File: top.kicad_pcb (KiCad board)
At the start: 2 copper layers, 98 x 50 mm, 4 parts, among them J2 Conn_01x01_Male, J5 Conn_01x01_Male, J7 Conn_01x01_Male, J9 Conn_01x01_Male

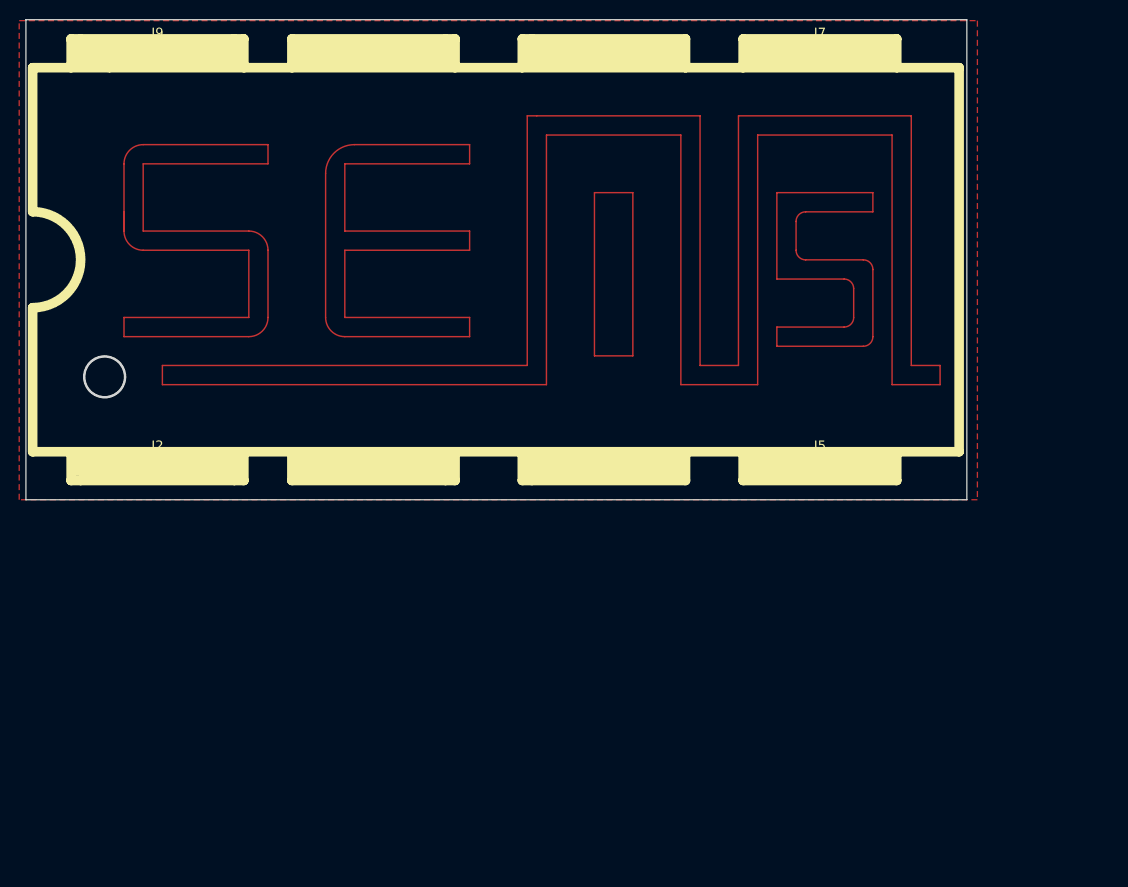
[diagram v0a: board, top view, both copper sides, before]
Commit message: top add silkscreen and fill other side
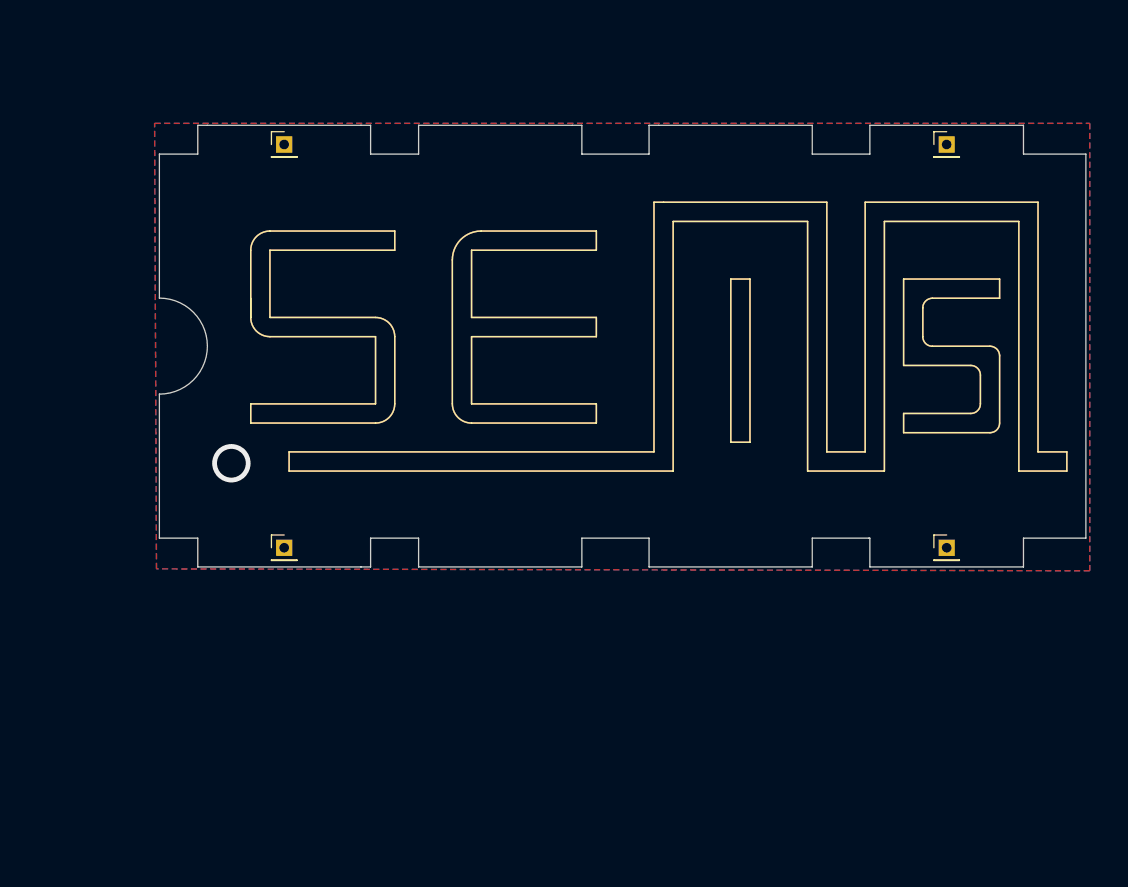
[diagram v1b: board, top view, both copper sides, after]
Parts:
- moved J9 16.1 mm to (95.7, 60.0)
- moved J7 16.1 mm to (164.7, 60.0)
- moved J2 15.6 mm to (95.7, 102.0)
- moved J5 15.6 mm to (164.7, 102.0)
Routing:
- added copper zone on B.Cu, net (none)
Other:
- board size 98 x 50 mm -> 96.5 x 46 mm

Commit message: gerberek, bom
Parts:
- added T1: Tab, kikit:Tab, F.Cu at (82.2, 68.0)
- added T1: Tab, kikit:Tab, F.Cu at (164.8, 57.6)
- added T1: Tab, kikit:Tab, F.Cu at (82.2, 94.0)
- added T1: Tab, kikit:Tab, F.Cu at (179.8, 94.0)
- added T1: Tab, kikit:Tab, F.Cu at (95.8, 57.6)
- added T1: Tab, kikit:Tab, F.Cu at (95.8, 104.3)
- added T1: Tab, kikit:Tab, F.Cu at (164.8, 104.3)
- added T1: Tab, kikit:Tab, F.Cu at (179.6, 68.4)
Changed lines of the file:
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@@
     )
+  )
+  (footprint "kikit:Tab" (layer "F.Cu")
+    (at 82.25 68)
+    (descr "A symbol representing annotation for tab placement")
+    (property "Sheetfile" "SEM15.kicad_sch")
+    (property "Sheetname" "")
+    (property "exclude_from_bom" "")
+    (property "ki_description" "KiKit tab annotations")
+    (property "ki_keywords" "KiKit")
+    (attr exclude_from_pos_files exclude_from_bom)
+    (fp_text reference "T1" (at 0 -2) (layer "F.SilkS") hide
+        (effects (font (size 1 1) (thickness 0.15)))
+    )
+    (fp_text value "Tab" (at -2.75 -1) (layer "Dwgs.User")
+        (effects (font (size 1.2 1.2) (thickness 0.2)))
+    )
+    (fp_text user "KIKIT: width: 3mm" (at -5.5 0 90) (layer "Dwgs.User")
+        (effects (font (size 1 1) (thickness 0.15)))
+    )
+    (fp_line (start 0.25 0) (end -2.75 0)
+      (stroke (width 0.3) (type solid)) (layer "Dwgs.User"))
+    (fp_line (start 0.25 0) (end -0.75 -1)
+      (stroke (width 0.3) (type solid)) (layer "Dwgs.User"))
+    (fp_line (start 0.25 0) (end -0.75 1)
+      (stroke (width 0.3) (type solid)) (layer "Dwgs.User"))
+    (fp_line (start 0.25 1) (end 0.25 -1)
+      (stroke (width 0.3) (type solid)) (layer "Dwgs.User"))
+  )
+  (footprint "kikit:Tab" (layer "F.Cu")
+    (at 164.8 57.65 -90)
+    (descr "A symbol representing annotation for tab placement")
+    (property "Sheetfile" "SEM15.kicad_sch")
+    (property "Sheetname" "")
+    (property "exclude_from_bom" "")
+    (property "ki_description" "KiKit tab annotations")
+    (property "ki_keywords" "KiKit")
+    (attr exclude_from_pos_files exclude_from_bom)
+    (fp_text reference "T1" (at 0 -2 90) (layer "F.SilkS") hide
+        (effects (font (size 1 1) (thickness 0.15)))
+    )
+    (fp_text value "Tab" (at -2.75 -1 90) (layer "Dwgs.User")
+        (effects (font (size 1.2 1.2) (thickness 0.2)))
+    )
+    (fp_text user "KIKIT: width: 3mm" (at -5.5 0) (layer "Dwgs.User")
+        (effects (font (size 1 1) (thickness 0.15)))
+    )
+    (fp_line (start 0.25 0) (end -2.75 0)
+      (stroke (width 0.3) (type solid)) (layer "Dwgs.User"))
+    (fp_line (start 0.25 0) (end -0.75 -1)
+      (stroke (width 0.3) (type solid)) (layer "Dwgs.User"))
+    (fp_line (start 0.25 0) (end -0.75 1)
+      (stroke (width 0.3) (type solid)) (layer "Dwgs.User"))
+    (fp_line (start 0.25 1) (end 0.25 -1)
+      (stroke (width 0.3) (type solid)) (layer "Dwgs.User"))
+  )
+  (footprint "kikit:Tab" (layer "F.Cu")
+    (at 82.25 94)
+    (descr "A symbol representing annotation for tab placement")
+    (property "Sheetfile" "SEM15.kicad_sch")
+    (property "Sheetname" "")
+    (property "exclude_from_bom" "")
+    (property "ki_description" "KiKit tab annotations")
+    (property "ki_keywords" "KiKit")
+    (attr exclude_from_pos_files exclude_from_bom)
+    (fp_text reference "T1" (at 0 -2) (layer "F.SilkS") hide
+        (effects (font (size 1 1) (thickness 0.15)))
+    )
+    (fp_text value "Tab" (at -2.75 -1) (layer "Dwgs.User")
+        (effects (font (size 1.2 1.2) (thickness 0.2)))
+    )
+    (fp_text user "KIKIT: width: 3mm" (at -5.5 0 90) (layer "Dwgs.User")
+        (effects (font (size 1 1) (thickness 0.15)))
+    )
+    (fp_line (start 0.25 0) (end -2.75 0)
+      (stroke (width 0.3) (type solid)) (layer "Dwgs.User"))
+    (fp_line (start 0.25 0) (end -0.75 -1)
+      (stroke (width 0.3) (type solid)) (layer "Dwgs.User"))
+    (fp_line (start 0.25 0) (end -0.75 1)
+      (stroke (width 0.3) (type solid)) (layer "Dwgs.User"))
+    (fp_line (start 0.25 1) (end 0.25 -1)
+      (stroke (width 0.3) (type solid)) (layer "Dwgs.User"))
+  )
+  (footprint "kikit:Tab" (layer "F.Cu")
+    (at 179.75 94 180)
+    (descr "A symbol representing annotation for tab placement")
+    (property "Sheetfile" "SEM15.kicad_sch")
+    (property "Sheetname" "")
+    (property "exclude_from_bom" "")
+    (property "ki_description" "KiKit tab annotations")
+    (property "ki_keywords" "KiKit")
+    (attr exclude_from_pos_files exclude_from_bom)
+    (fp_text reference "T1" (at 0 -2) (layer "F.SilkS") hide
+        (effects (font (size 1 1) (thickness 0.15)))
+    )
+    (fp_text value "Tab" (at -2.75 -1) (layer "Dwgs.User")
+        (effects (font (size 1.2 1.2) (thickness 0.2)))
+    )
+    (fp_text user "KIKIT: width: 3mm" (at -5.5 0 90) (layer "Dwgs.User")
+        (effects (font (size 1 1) (thickness 0.15)))
+    )
+    (fp_line (start 0.25 0) (end -2.75 0)
+      (stroke (width 0.3) (type solid)) (layer "Dwgs.User"))
+    (fp_line (start 0.25 0) (end -0.75 -1)
+      (stroke (width 0.3) (type solid)) (layer "Dwgs.User"))
+    (fp_line (start 0.25 0) (end -0.75 1)
+      (stroke (width 0.3) (type solid)) (layer "Dwgs.User"))
+    (fp_line (start 0.25 1) (end 0.25 -1)
+      (stroke (width 0.3) (type solid)) (layer "Dwgs.User"))
   )
   (footprint "Connector_PinHeader_2.54mm:PinHeader_1x01_P2.54mm_Vertical" (layer "F.Cu")
@@
     )
   )
+  (footprint "kikit:Tab" (layer "F.Cu")
+    (at 95.8 57.65 -90)
+    (descr "A symbol representing annotation for tab placement")
+    (property "Sheetfile" "SEM15.kicad_sch")
+    (property "Sheetname" "")
+    (property "exclude_from_bom" "")
+    (property "ki_description" "KiKit tab annotations")
+    (property "ki_keywords" "KiKit")
+    (attr exclude_from_pos_files exclude_from_bom)
+    (fp_text reference "T1" (at 0 -2 90) (layer "F.SilkS") hide
+        (effects (font (size 1 1) (thickness 0.15)))
+    )
+    (fp_text value "Tab" (at -2.75 -1 90) (layer "Dwgs.User")
+        (effects (font (size 1.2 1.2) (thickness 0.2)))
+    )
+    (fp_text user "KIKIT: width: 3mm" (at -5.5 0) (layer "Dwgs.User")
+        (effects (font (size 1 1) (thickness 0.15)))
+    )
+    (fp_line (start 0.25 0) (end -2.75 0)
+      (stroke (width 0.3) (type solid)) (layer "Dwgs.User"))
+    (fp_line (start 0.25 0) (end -0.75 -1)
+      (stroke (width 0.3) (type solid)) (layer "Dwgs.User"))
+    (fp_line (start 0.25 0) (end -0.75 1)
+      (stroke (width 0.3) (type solid)) (layer "Dwgs.User"))
+    (fp_line (start 0.25 1) (end 0.25 -1)
+      (stroke (width 0.3) (type solid)) (layer "Dwgs.User"))
+  )
   (footprint "Connector_PinHeader_2.54mm:PinHeader_1x01_P2.54mm_Vertical" (layer "F.Cu")
     (at 95.7 102)
@@
     )
   )
+  (footprint "kikit:Tab" (layer "F.Cu")
+    (at 95.8 104.35 90)
+    (descr "A symbol representing annotation for tab placement")
+    (property "Sheetfile" "SEM15.kicad_sch")
+    (property "Sheetname" "")
+    (property "exclude_from_bom" "")
+    (property "ki_description" "KiKit tab annotations")
+    (property "ki_keywords" "KiKit")
+    (attr exclude_from_pos_files exclude_from_bom)
+    (fp_text reference "T1" (at 0 -2 90) (layer "F.SilkS") hide
+        (effects (font (size 1 1) (thickness 0.15)))
+    )
+    (fp_text value "Tab" (at -2.75 -1 90) (layer "Dwgs.User")
+        (effects (font (size 1.2 1.2) (thickness 0.2)))
+    )
+    (fp_text user "KIKIT: width: 3mm" (at -5.5 0) (layer "Dwgs.User")
+        (effects (font (size 1 1) (thickness 0.15)))
+    )
+    (fp_line (start 0.25 0) (end -2.75 0)
+      (stroke (width 0.3) (type solid)) (layer "Dwgs.User"))
+    (fp_line (start 0.25 0) (end -0.75 -1)
+      (stroke (width 0.3) (type solid)) (layer "Dwgs.User"))
+    (fp_line (start 0.25 0) (end -0.75 1)
+      (stroke (width 0.3) (type solid)) (layer "Dwgs.User"))
+    (fp_line (start 0.25 1) (end 0.25 -1)
+      (stroke (width 0.3) (type solid)) (layer "Dwgs.User"))
+  )
+  (footprint "kikit:Tab" (layer "F.Cu")
+    (at 164.8 104.35 90)
+    (descr "A symbol representing annotation for tab placement")
+    (property "Sheetfile" "SEM15.kicad_sch")
+    (property "Sheetname" "")
+    (property "exclude_from_bom" "")
+    (property "ki_description" "KiKit tab annotations")
+    (property "ki_keywords" "KiKit")
+    (attr exclude_from_pos_files exclude_from_bom)
+    (fp_text reference "T1" (at 0 -2 90) (layer "F.SilkS") hide
+        (effects (font (size 1 1) (thickness 0.15)))
+    )
+    (fp_text value "Tab" (at -2.75 -1 90) (layer "Dwgs.User")
+        (effects (font (size 1.2 1.2) (thickness 0.2)))
+    )
+    (fp_text user "KIKIT: width: 3mm" (at -5.5 0) (layer "Dwgs.User")
+        (effects (font (size 1 1) (thickness 0.15)))
+    )
+    (fp_line (start 0.25 0) (end -2.75 0)
+      (stroke (width 0.3) (type solid)) (layer "Dwgs.User"))
+    (fp_line (start 0.25 0) (end -0.75 -1)
+      (stroke (width 0.3) (type solid)) (layer "Dwgs.User"))
+    (fp_line (start 0.25 0) (end -0.75 1)
+      (stroke (width 0.3) (type solid)) (layer "Dwgs.User"))
+    (fp_line (start 0.25 1) (end 0.25 -1)
+      (stroke (width 0.3) (type solid)) (layer "Dwgs.User"))
+  )
+  (footprint "kikit:Tab" (layer "F.Cu")
+    (at 179.55 68.4 180)
+    (descr "A symbol representing annotation for tab placement")
+    (property "Sheetfile" "SEM15.kicad_sch")
+    (property "Sheetname" "")
+    (property "exclude_from_bom" "")
+    (property "ki_description" "KiKit tab annotations")
+    (property "ki_keywords" "KiKit")
+    (attr exclude_from_pos_files exclude_from_bom)
+    (fp_text reference "T1" (at 0 -2) (layer "F.SilkS") hide
+        (effects (font (size 1 1) (thickness 0.15)))
+    )
+    (fp_text value "Tab" (at -2.75 -1) (layer "Dwgs.User")
+        (effects (font (size 1.2 1.2) (thickness 0.2)))
+    )
+    (fp_text user "KIKIT: width: 3mm" (at -5.5 0 90) (layer "Dwgs.User")
+        (effects (font (size 1 1) (thickness 0.15)))
+    )
+    (fp_line (start 0.25 0) (end -2.75 0)
+      (stroke (width 0.3) (type solid)) (layer "Dwgs.User"))
+    (fp_line (start 0.25 0) (end -0.75 -1)
+      (stroke (width 0.3) (type solid)) (layer "Dwgs.User"))
+    (fp_line (start 0.25 0) (end -0.75 1)
+      (stroke (width 0.3) (type solid)) (layer "Dwgs.User"))
+    (fp_line (start 0.25 1) (end 0.25 -1)
+      (stroke (width 0.3) (type solid)) (layer "Dwgs.User"))
+  )
   (gr_line (start 156.214214 92.014214) (end 156.214214 66.014214)

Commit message: sent to jlc
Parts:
- removed the T1 at (82.2, 68.0)
- removed the T1 at (164.8, 57.6)
- removed the T1 at (82.2, 94.0)
- removed the T1 at (179.8, 94.0)
- removed the T1 at (95.8, 57.6)
- removed the T1 at (95.8, 104.3)
- removed the T1 at (164.8, 104.3)
- removed the T1 at (179.6, 68.4)
- added T1: Tab, kikit:Tab, F.Cu at (84.2, 98.9)
- added T1: Tab, kikit:Tab, F.Cu at (181.5, 99.3)
- added T1: Tab, kikit:Tab, F.Cu at (181.7, 124.9)
- added T1: Tab, kikit:Tab, F.Cu at (166.8, 88.5)
- added T1: Tab, kikit:Tab, F.Cu at (97.8, 135.2)
- added T1: Tab, kikit:Tab, F.Cu at (84.2, 124.9)
- added T1: Tab, kikit:Tab, F.Cu at (97.8, 88.5)
- added T1: Tab, kikit:Tab, F.Cu at (166.8, 135.2)
- moved J2 30.9 mm to (97.7, 132.9)
- moved J5 30.9 mm to (166.7, 132.9)
- moved J7 30.9 mm to (166.7, 90.9)
- moved J9 30.9 mm to (97.7, 90.9)
